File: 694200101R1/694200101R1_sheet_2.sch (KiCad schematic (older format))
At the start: 89 parts, among them U4 M24M02-DRMN6TP, U5 IS31FL3733B-QFLS4-TR, U6 IS31FL3733B-QFLS4-TR

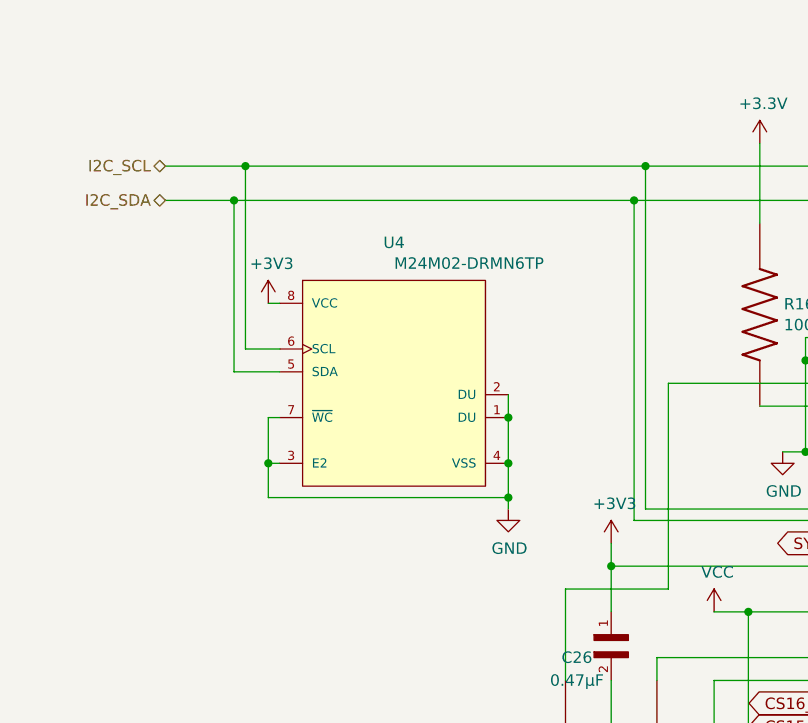
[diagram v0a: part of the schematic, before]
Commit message: Added Smaller EEPROM for QMK
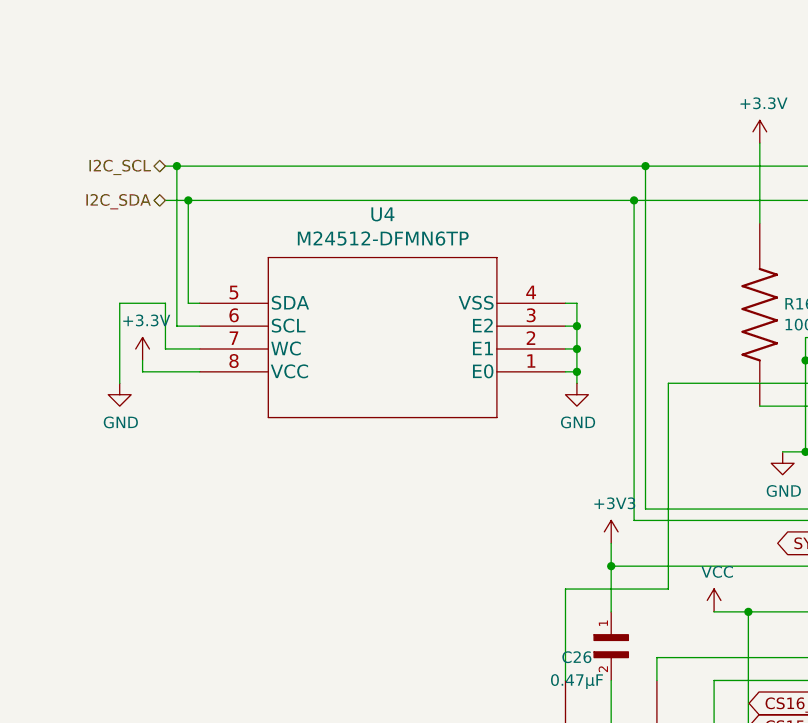
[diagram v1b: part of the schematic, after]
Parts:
- removed U4: M24M02-DRMN6TP, STM:STMicroelectronics-SO8N-SO-A-0-2-IPC_C, symbol STM:M24M02-DRMN6TP
- added U4: M24512-DFMN6TP, STM:STMicroelectronics-SO8N-SO-A-0-2-MFG, symbol STM_EEPROM:M24512-DFMN6TP
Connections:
- net +3V3: now also U4.8 (VCC)
- net GND: now also U4.1 (E0), U4.2 (E1), U4.3 (E2), U4.4 (VSS), U4.7 (WC)
- net I2C_SCL: now also U4.6 (SCL)
- net I2C_SDA: now also U4.5 (SDA)
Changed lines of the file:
@@
 I2C_SCL
 Wire Wire Line
-	1550 7900 1350 7900
-Wire Wire Line
-	1400 7800 1550 7800
-Wire Wire Line
-	1550 7600 1500 7600
-Wire Wire Line
-	2550 8000 2550 8100
-Wire Wire Line
-	2550 8100 2550 8300
-Connection ~ 2550 8100
-Wire Wire Line
-	1550 8100 1500 8100
-Wire Wire Line
-	1500 8100 1500 8300
-Wire Wire Line
-	1500 8300 1550 8300
-Wire Wire Line
-	1500 8300 1500 8450
-Wire Wire Line
-	1500 8450 2550 8450
-Wire Wire Line
-	2550 8450 2550 8300
-Connection ~ 1500 8300
-Connection ~ 2550 8300
-Connection ~ 2550 8450
-Wire Wire Line
 	3100 8550 4000 8550
 Wire Wire Line
@@
 Connection ~ 8050 8450
 Wire Wire Line
-	2550 8450 2550 8500
-Wire Wire Line
 	1000 1000 900  1000
 Wire Wire Line
@@
 Connection ~ 6550 1200
 $Comp
-L STM:M24M02-DRMN6TP U4
-U 1 1 63D31709
-P 1450 7600
-F 0 "U4" H 2050 7865 50  0000 C CNN
-F 1 "M24M02-DRMN6TP" H 2050 7774 50  0000 L CNN
-F 2 "STM:STMicroelectronics-SO8N-SO-A-0-2-IPC_C" H 1450 8000 50  0001 L CNN
-F 3 "https://www.st.com/resource/en/datasheet/m24m02-dr.pdf" H 1450 8100 50  0001 L CNN
-F 4 "450ns" H 1450 8200 50  0001 L CNN "access time"
-F 5 "+85°C" H 1450 8300 50  0001 L CNN "ambient temperature range high"
-F 6 "-40°C" H 1450 8400 50  0001 L CNN "ambient temperature range low"
-F 7 "No" H 1450 8500 50  0001 L CNN "automotive"
-F 8 "IC" H 1450 8600 50  0001 L CNN "category"
-F 9 "Integrated Circuits (ICs)" H 1450 8700 50  0001 L CNN "device class L1"
-F 10 "Memory" H 1450 8800 50  0001 L CNN "device class L2"
-F 11 "EEPROM" H 1450 8900 50  0001 L CNN "device class L3"
-F 12 "IC EEPROM 2M I2C 1MHZ 8SO" H 1450 9000 50  0001 L CNN "digikey description"
-F 13 "497-11600-1-ND" H 1450 9100 50  0001 L CNN "digikey part number"
-F 14 "1MHz" H 1450 9200 50  0001 L CNN "frequency"
-F 15 "1.75mm" H 1450 9300 50  0001 L CNN "height"
-F 16 "I2C" H 1450 9400 50  0001 L CNN "interface"
-F 17 "Yes" H 1450 9500 50  0001 L CNN "lead free"
-F 18 "2c41b2375d0f4e7f" H 1450 9600 50  0001 L CNN "library id"
-F 19 "STMicroelectronics" H 1450 9700 50  0001 L CNN "manufacturer"
-F 20 "5.5V" H 1450 9800 50  0001 L CNN "max supply voltage"
-F 21 "2Mbits" H 1450 9900 50  0001 L CNN "memory size"
-F 22 "EEPROM" H 1450 10000 50  0001 L CNN "memory type"
-F 23 "1.8V" H 1450 10100 50  0001 L CNN "min supply voltage"
-F 24 "EEPROM 2 Mbit serial I2C 1.8V to 5.5V EEPROM\\n" H 1450 10200 50  0001 L CNN "mouser description"
-F 25 "511-M24M02-DRMN6TP" H 1450 10300 50  0001 L CNN "mouser part number"
-F 26 "1-2.5mA" H 1450 10400 50  0001 L CNN "nominal supply current"
-F 27 "SO-8" H 1450 10500 50  0001 L CNN "package"
-F 28 "Yes" H 1450 10600 50  0001 L CNN "rohs"
-F 29 "0.1mm" H 1450 10700 50  0001 L CNN "standoff height"
-F 30 "+85°C" H 1450 10800 50  0001 L CNN "temperature range high"
-F 31 "-40°C" H 1450 10900 50  0001 L CNN "temperature range low"
-	1    1450 7600
-	1    0    0    -1
-$EndComp
-$Comp
-L power:+3V3 #PWR017
-U 1 1 63D43A95
-P 1500 7600
-F 0 "#PWR017" H 1500 7450 50  0001 C CNN
-F 1 "+3V3" H 1515 7773 50  0000 C CNN
-F 2 "" H 1500 7600 50  0001 C CNN
-F 3 "" H 1500 7600 50  0001 C CNN
-	1    1500 7600
-	1    0    0    -1
-$EndComp
-$Comp
-L power:GND #PWR018
-U 1 1 63D489E9
-P 2550 8500
-F 0 "#PWR018" H 2550 8250 50  0001 C CNN
-F 1 "GND" H 2555 8327 50  0000 C CNN
-F 2 "" H 2550 8500 50  0001 C CNN
-F 3 "" H 2550 8500 50  0001 C CNN
-	1    2550 8500
-	1    0    0    -1
-$EndComp
-$Comp
 L Lumissil:IS31FL3733B-QFLS4-TR U5
 U 1 1 63D4A2BB
@@
 	7200 7150 7200 8550
 Wire Wire Line
-	1050 7150 1350 7150
-Wire Wire Line
-	1350 7150 1350 7900
-Connection ~ 1350 7150
-Wire Wire Line
-	1350 7150 3100 7150
-Wire Wire Line
 	3100 7150 3100 8550
 Connection ~ 3100 7150
@@
 	7250 7000 7250 8500
 Wire Wire Line
-	1050 7000 1400 7000
-Wire Wire Line
-	1400 7000 1400 7800
-Connection ~ 1400 7000
-Wire Wire Line
 	3150 7000 3150 8500
-Wire Wire Line
-	1400 7000 3150 7000
 Connection ~ 3150 7000
 Wire Wire Line
@@
 P 13100 6800
 AR Path="/6364BAD2" Ref="#PWR?"  Part="1"
-AR Path="/63A35802/6364BAD2" Ref="#PWR?"  Part="1"
-F 0 "#PWR?" H 13100 6650 50  0001 C CNN
+AR Path="/63A35802/6364BAD2" Ref="#PWR017"  Part="1"
+F 0 "#PWR017" H 13100 6650 50  0001 C CNN
 F 1 "VCC" H 13115 6973 50  0000 C CNN
 F 2 "" H 13100 6800 50  0001 C CNN
@@
 Wire Wire Line
 	13100 6900 13100 6800
+$Comp
+L STM_EEPROM:M24512-DFMN6TP U4
+U 1 1 60F1F6EF
+P 2800 7900
+F 0 "U4" H 3600 7213 60  0000 C CNN
+F 1 "M24512-DFMN6TP" H 3600 7319 60  0000 C CNN
+F 2 "STM:STMicroelectronics-SO8N-SO-A-0-2-MFG" H 3600 8140 60  0001 C CNN
+F 3 "" H 2800 7900 60  0000 C CNN
+	1    2800 7900
+	-1   0    0    1
+$EndComp
+Wire Wire Line
+	1050 7000 1100 7000
+Wire Wire Line
+	1050 7150 1150 7150
+Wire Wire Line
+	1100 7000 1100 7700
+Wire Wire Line
+	1100 7700 1200 7700
+Connection ~ 1100 7000
+Wire Wire Line
+	1100 7000 3150 7000
+Wire Wire Line
+	1150 7150 1150 7600
+Wire Wire Line
+	1150 7600 1200 7600
+Connection ~ 1150 7150
+Wire Wire Line
+	1150 7150 3100 7150
+Wire Wire Line
+	2800 7600 2850 7600
+Wire Wire Line
+	2850 7600 2850 7700
+Wire Wire Line
+	2800 7700 2850 7700
+Connection ~ 2850 7700
+Wire Wire Line
+	2850 7700 2850 7800
+Wire Wire Line
+	2800 7800 2850 7800
+Connection ~ 2850 7800
+Wire Wire Line
+	2850 7800 2850 7900
+Wire Wire Line
+	2800 7900 2850 7900
+Connection ~ 2850 7900
+Wire Wire Line
+	2850 7900 2850 7950
+Wire Wire Line
+	1200 7800 1050 7800
+Wire Wire Line
+	1050 7800 1050 7600
+Wire Wire Line
+	850  7600 850  7950
+Wire Wire Line
+	850  7600 1050 7600
+$Comp
+L power:GND #PWR02
+U 1 1 6163A9DA
+P 850 7950
+F 0 "#PWR02" H 850 7700 50  0001 C CNN
+F 1 "GND" H 855 7777 50  0000 C CNN
+F 2 "" H 850 7950 50  0001 C CNN
+F 3 "" H 850 7950 50  0001 C CNN
+	1    850  7950
+	1    0    0    -1
+$EndComp
+$Comp
+L power:+3.3V #PWR05
+U 1 1 6163D8D2
+P 950 7850
+F 0 "#PWR05" H 950 7700 50  0001 C CNN
+F 1 "+3.3V" H 965 8023 50  0000 C CNN
+F 2 "" H 950 7850 50  0001 C CNN
+F 3 "" H 950 7850 50  0001 C CNN
+	1    950  7850
+	1    0    0    -1
+$EndComp
+Wire Wire Line
+	1200 7900 950  7900
+Wire Wire Line
+	950  7900 950  7850
+$Comp
+L power:GND #PWR06
+U 1 1 61F36928
+P 2850 7950
+F 0 "#PWR06" H 2850 7700 50  0001 C CNN
+F 1 "GND" H 2855 7777 50  0000 C CNN
+F 2 "" H 2850 7950 50  0001 C CNN
+F 3 "" H 2850 7950 50  0001 C CNN
+	1    2850 7950
+	1    0    0    -1
+$EndComp
 $EndSCHEMATC
